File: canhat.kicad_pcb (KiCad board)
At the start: 2 copper layers, 65 x 30 mm, 25 parts, among them J1 Raspberry_Pi_2_3, J2 CAN In / Out, J3 5V, U1 MCP2515-xSO, U2 SN65HVD234, U3 AT24C32-SSHM, Y1 16MHz

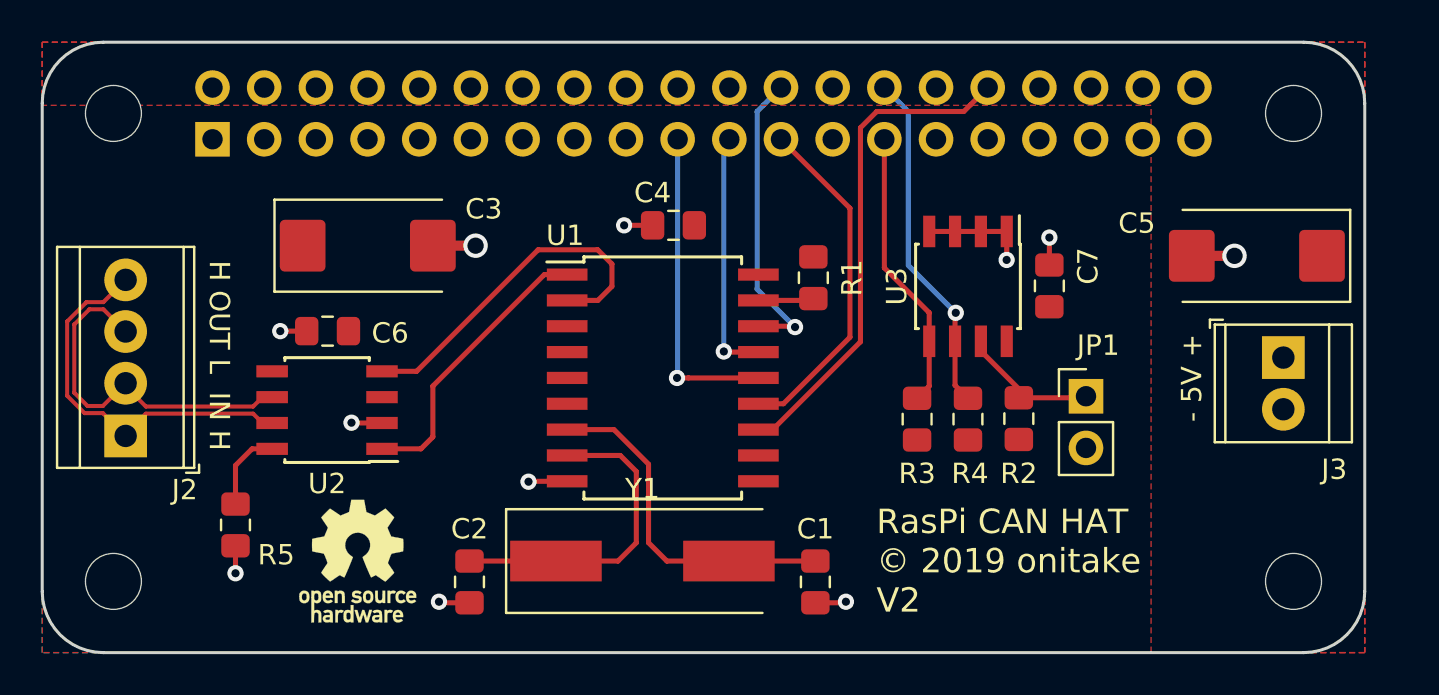
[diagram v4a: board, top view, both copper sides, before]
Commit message: Split off power plane for transceiver for 3.3/5V power
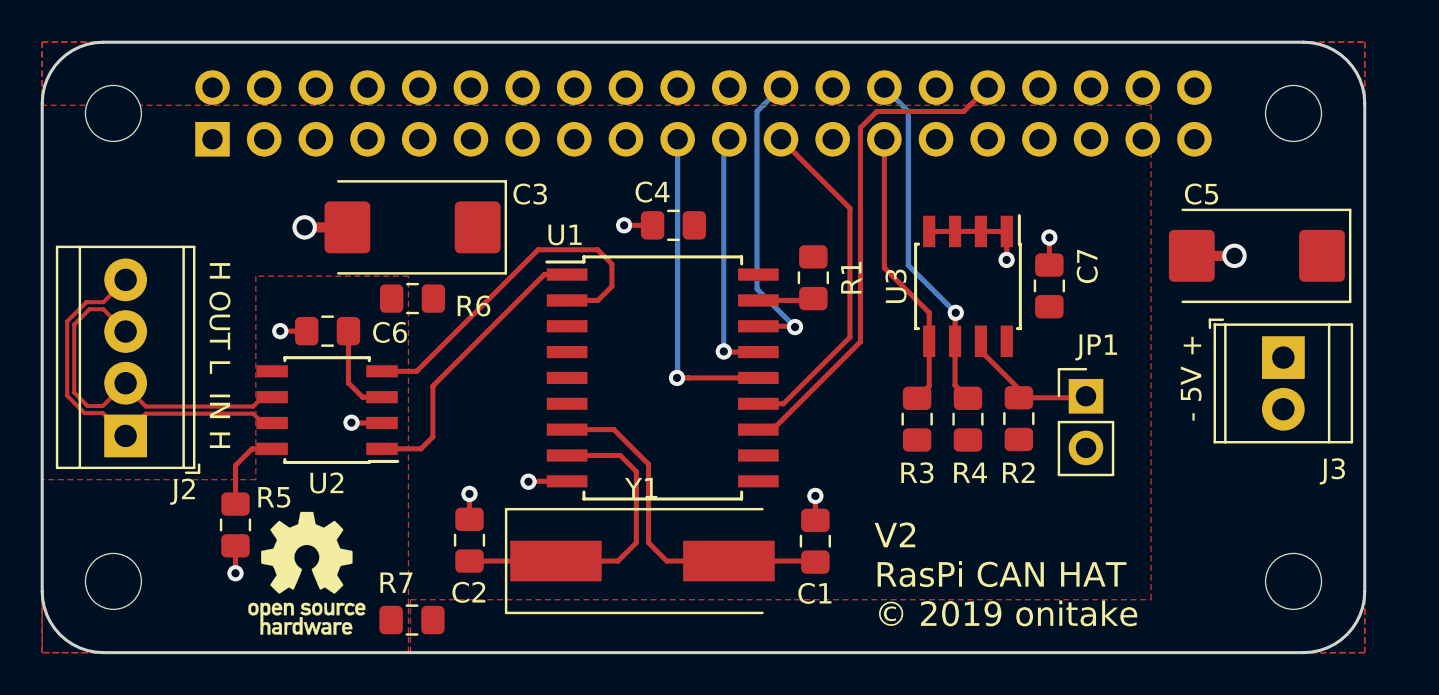
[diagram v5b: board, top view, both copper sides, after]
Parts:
- added R6: DNP/0, Resistor_SMD:R_0805_2012Metric_Pad1.15x1.40mm_HandSolder, F.Cu at (58.2, 62.6)
- added R7: 0/DNP, Resistor_SMD:R_0805_2012Metric_Pad1.15x1.40mm_HandSolder, F.Cu at (58.2, 78.4)
- moved OSHW1 2.57 mm to (53.0, 76.1)
- moved C3 2.38 mm to (58.2, 59.1), turned to 180 degrees
- moved C2 2.05 mm to (61.0, 74.5), turned to 270 degrees
- moved C1 2.00 mm to (78.0, 74.5), turned to 90 degrees
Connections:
- C6 pad 1: +3V3 -> VBUS
- U2 pad 3: +3V3 -> VBUS
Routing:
- net VBUS: track 0.00 -> 4.49 mm
- net GND: track 21.3 -> 20.7 mm
- added copper zone on F.Cu, net VBUS
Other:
- board text added: "V2 RasPi CAN HAT © 2019 onitake"
- board text removed: "RasPi CAN HAT © 2019 onitake V2"

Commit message: Non-planar Vcc/Vbus wiring
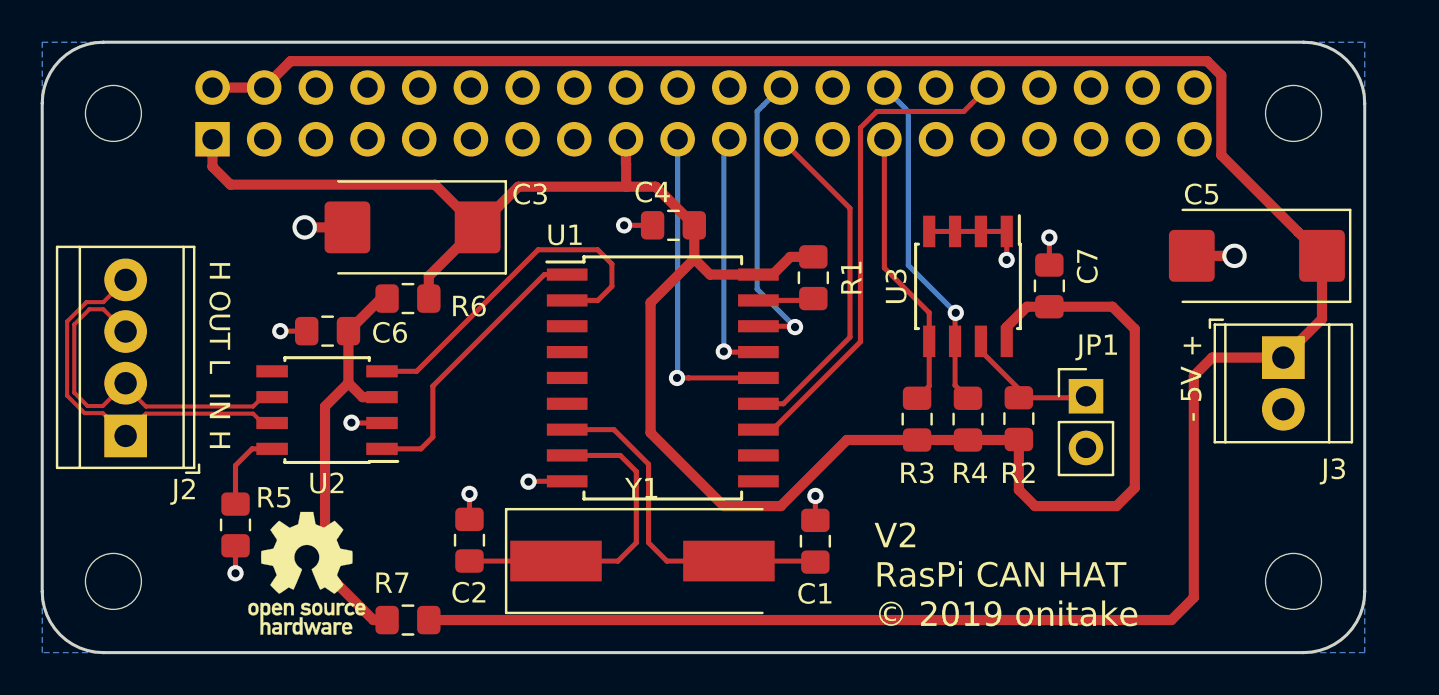
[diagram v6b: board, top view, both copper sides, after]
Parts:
- moved R6 0.23 mm to (58.0, 62.6)
- moved R7 0.20 mm to (58.0, 78.4)
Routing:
- net +5V: track 0.00 -> 120.8 mm
- net +3V3: track 0.00 -> 97.8 mm
- net VBUS: track 4.49 -> 20.8 mm
- removed copper zone on F.Cu, net +3V3
- removed copper zone on F.Cu, net +5V
- removed copper zone on F.Cu, net VBUS
